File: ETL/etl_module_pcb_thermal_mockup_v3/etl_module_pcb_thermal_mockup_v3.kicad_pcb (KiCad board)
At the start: 2 copper layers, 44.1 x 57.5 mm, 21 parts, among them J1 WP7B-S050VA1-R8000, J2 WP7B-S050VA1-R8000, J3 Conn_02x02_Odd_Even, J4 Conn_02x08_Counter_Clockwise, J5 Conn_02x08_Counter_Clockwise, J6 Conn_02x08_Counter_Clockwise, J7 Conn_02x08_Counter_Clockwise

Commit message: Progress on etl_module_pcb_thermal_mcokup_v3
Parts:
- removed X1: , unl_silab:PCB_ETROC2_dummy
- added U1: ETROC_dummy_thermal_sensors, unl_silab:PCB_ETROC2_dummy, F.Cu at (11.2, 50.7)
- moved J7 24.2 mm to (33.3, 16.8)
- moved J4 19.4 mm to (9.40, 43.5)
- moved J6 18.2 mm to (11.4, 16.9)
- moved J5 8.65 mm to (33.2, 42.7)
- renumbered X2 to U2, X3 to U3, X4 to U4
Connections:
- J1 pad 10: /30_N -> unconnected-(J1-Pad10)
- J1 pad 11: /31_P -> unconnected-(J1-Pad11)
- J1 pad 12: /31_N -> unconnected-(J1-Pad12)
- J1 pad 13: /32_P -> unconnected-(J1-Pad13)
- J1 pad 14: /32_N -> unconnected-(J1-Pad14)
- J1 pad 15: /33_P -> unconnected-(J1-Pad15)
- J1 pad 16: /33_N -> unconnected-(J1-Pad16)
- J1 pad 17: /34_P -> unconnected-(J1-Pad17)
- J1 pad 18: /34_N -> unconnected-(J1-Pad18)
- J1 pad 19: /35_P -> unconnected-(J1-Pad19)
- J1 pad 2: /26_N -> unconnected-(J1-Pad2)
- J1 pad 20: /35_N -> unconnected-(J1-Pad20)
- J1 pad 21: /36_P -> unconnected-(J1-Pad21)
- J1 pad 22: /36_N -> unconnected-(J1-Pad22)
- J1 pad 23: /37_P -> unconnected-(J1-Pad23)
- J1 pad 24: /37_N -> unconnected-(J1-Pad24)
- J1 pad 25: /38_P -> unconnected-(J1-Pad25)
- J1 pad 26: /38_N -> unconnected-(J1-Pad26)
- J1 pad 27: /39_P -> unconnected-(J1-Pad27)
- J1 pad 28: /39_N -> unconnected-(J1-Pad28)
- J1 pad 29: /40_P -> unconnected-(J1-Pad29)
- J1 pad 3: /27_P -> unconnected-(J1-Pad3)
- J1 pad 30: /40_N -> unconnected-(J1-Pad30)
- J1 pad 31: /41_P -> unconnected-(J1-Pad31)
- J1 pad 32: /41_N -> unconnected-(J1-Pad32)
- J1 pad 33: /42_P -> unconnected-(J1-Pad33)
- J1 pad 34: /42_N -> unconnected-(J1-Pad34)
- J1 pad 35: /43_P -> unconnected-(J1-Pad35)
- J1 pad 36: /43_N -> unconnected-(J1-Pad36)
- J1 pad 37: /44_P -> unconnected-(J1-Pad37)
- J1 pad 38: /44_N -> unconnected-(J1-Pad38)
- J1 pad 39: /45_P -> unconnected-(J1-Pad39)
- J1 pad 4: /27_N -> unconnected-(J1-Pad4)
- J1 pad 40: /45_N -> unconnected-(J1-Pad40)
- J1 pad 41: /46_P -> unconnected-(J1-Pad41)
- J1 pad 42: /46_N -> unconnected-(J1-Pad42)
- J1 pad 43: /47_P -> unconnected-(J1-Pad43)
- J1 pad 44: /47_N -> unconnected-(J1-Pad44)
- J1 pad 45: /48_P -> unconnected-(J1-Pad45)
- J1 pad 46: /48_N -> unconnected-(J1-Pad46)
- J1 pad 47: /49_P -> unconnected-(J1-Pad47)
- J1 pad 48: /49_N -> unconnected-(J1-Pad48)
- J1 pad 49: /S2 -> unconnected-(J1-Pad49)
- J1 pad 5: /28_P -> unconnected-(J1-Pad5)
- J1 pad 50: /S2 -> unconnected-(J1-Pad50)
- J1 pad 6: /28_N -> unconnected-(J1-Pad6)
- J1 pad 7: /29_P -> unconnected-(J1-Pad7)
- J1 pad 8: /29_N -> unconnected-(J1-Pad8)
- J1 pad 9: /30_P -> unconnected-(J1-Pad9)
- J2 pad 1: /01_N -> unconnected-(J2-Pad1)
- J2 pad 10: /05_P -> unconnected-(J2-Pad10)
- J2 pad 11: /06_N -> unconnected-(J2-Pad11)
- J2 pad 12: /06_P -> unconnected-(J2-Pad12)
- J2 pad 13: /07_N -> unconnected-(J2-Pad13)
- J2 pad 14: /07_P -> unconnected-(J2-Pad14)
- J2 pad 15: /08_N -> unconnected-(J2-Pad15)
- J2 pad 16: /08_P -> unconnected-(J2-Pad16)
- J2 pad 17: /09_N -> unconnected-(J2-Pad17)
- J2 pad 18: /09_P -> unconnected-(J2-Pad18)
- J2 pad 19: /10_N -> unconnected-(J2-Pad19)
- J2 pad 2: /01_P -> unconnected-(J2-Pad2)
- J2 pad 20: /10_P -> unconnected-(J2-Pad20)
- J2 pad 21: /11_N -> unconnected-(J2-Pad21)
- J2 pad 22: /11_P -> unconnected-(J2-Pad22)
- J2 pad 23: /12_N -> unconnected-(J2-Pad23)
- J2 pad 24: /12_P -> unconnected-(J2-Pad24)
- J2 pad 25: /13_N -> unconnected-(J2-Pad25)
- J2 pad 26: /13_P -> unconnected-(J2-Pad26)
- J2 pad 27: /14_N -> unconnected-(J2-Pad27)
- J2 pad 28: /14_P -> unconnected-(J2-Pad28)
- J2 pad 29: /15_N -> unconnected-(J2-Pad29)
- J2 pad 3: /02_N -> unconnected-(J2-Pad3)
- J2 pad 30: /15_P -> unconnected-(J2-Pad30)
- J2 pad 31: /16_N -> unconnected-(J2-Pad31)
- J2 pad 32: /16_P -> unconnected-(J2-Pad32)
- J2 pad 33: /17_N -> unconnected-(J2-Pad33)
- J2 pad 34: /17_P -> unconnected-(J2-Pad34)
- J2 pad 35: /18_N -> unconnected-(J2-Pad35)
- J2 pad 36: /18_P -> unconnected-(J2-Pad36)
- J2 pad 37: /19_N -> unconnected-(J2-Pad37)
- J2 pad 38: /19_P -> unconnected-(J2-Pad38)
- J2 pad 39: /20_N -> unconnected-(J2-Pad39)
- J2 pad 4: /02_P -> unconnected-(J2-Pad4)
- J2 pad 40: /20_P -> unconnected-(J2-Pad40)
- J2 pad 41: /21_N -> unconnected-(J2-Pad41)
- J2 pad 42: /21_P -> unconnected-(J2-Pad42)
- J2 pad 43: /22_N -> unconnected-(J2-Pad43)
- J2 pad 44: /22_P -> unconnected-(J2-Pad44)
- J2 pad 45: /23_N -> unconnected-(J2-Pad45)
- J2 pad 46: /23_P -> unconnected-(J2-Pad46)
- J2 pad 47: /24_N -> unconnected-(J2-Pad47)
- J2 pad 48: /24_P -> unconnected-(J2-Pad48)
- J2 pad 49: /S1 -> unconnected-(J2-Pad49)
- J2 pad 5: /03_N -> unconnected-(J2-Pad5)
- J2 pad 50: /S1 -> unconnected-(J2-Pad50)
- J2 pad 6: /03_P -> unconnected-(J2-Pad6)
- J2 pad 7: /04_N -> unconnected-(J2-Pad7)
- J2 pad 8: /04_P -> unconnected-(J2-Pad8)
- J2 pad 9: /05_N -> unconnected-(J2-Pad9)
- J4 pad 1: unconnected-(J4-Pad1) -> /X1EBR2
- J4 pad 10: unconnected-(J4-Pad10) -> /X1LBL1
- J4 pad 11: unconnected-(J4-Pad11) -> /X1LBR1
- J4 pad 12: unconnected-(J4-Pad12) -> /X1LBL2
- J4 pad 13: unconnected-(J4-Pad13) -> /X1LTR2
- J4 pad 14: unconnected-(J4-Pad14) -> /X1LTL1
- J4 pad 15: unconnected-(J4-Pad15) -> /X1LTR1
- J4 pad 16: unconnected-(J4-Pad16) -> /X1LTL2
- J4 pad 2: unconnected-(J4-Pad2) -> /X1EBL1
- J4 pad 3: unconnected-(J4-Pad3) -> /X1EBR1
- J4 pad 4: unconnected-(J4-Pad4) -> /X1EBL2
- J4 pad 5: unconnected-(J4-Pad5) -> /X1ETR2
- J4 pad 6: unconnected-(J4-Pad6) -> /X1ETL1
- J4 pad 7: unconnected-(J4-Pad7) -> /X1ETR1
- J4 pad 8: unconnected-(J4-Pad8) -> /X1ETL2
- J4 pad 9: unconnected-(J4-Pad9) -> /X1LBR2
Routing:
- net /P1: track 3430.2 -> 0.00 mm, vias 12 -> 0
- net unconnected-(J6-Pad10): track 0.00 -> 3378.6 mm, vias 0 -> 12
- net /X1EBL1: track 0.00 -> 19.0 mm, vias 0 -> 1
- net /X1EBR2: track 0.00 -> 18.8 mm, vias 0 -> 1
- net /X1ETR2: track 0.00 -> 17.4 mm, vias 0 -> 1
- net /X1EBR1: track 0.00 -> 17.3 mm, vias 0 -> 1
- net /X1EBL2: track 0.00 -> 17.0 mm, vias 0 -> 1
- net /X1ETL1: track 0.00 -> 16.2 mm, vias 0 -> 1
- net /X1ETR1: track 0.00 -> 14.1 mm, vias 0 -> 1
- net /X1LBR1: track 0.00 -> 13.0 mm, vias 0 -> 1
- net /X1ETL2: track 0.00 -> 13.0 mm, vias 0 -> 1
- net /X1LBR2: track 0.00 -> 12.7 mm, vias 0 -> 1
- net /X1LBL2: track 0.00 -> 12.1 mm, vias 0 -> 1
- net /X1LBL1: track 0.00 -> 11.6 mm, vias 0 -> 1
- net /X1LTR2: track 0.00 -> 8.83 mm, vias 0 -> 1
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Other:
- copper layers 2 -> 4

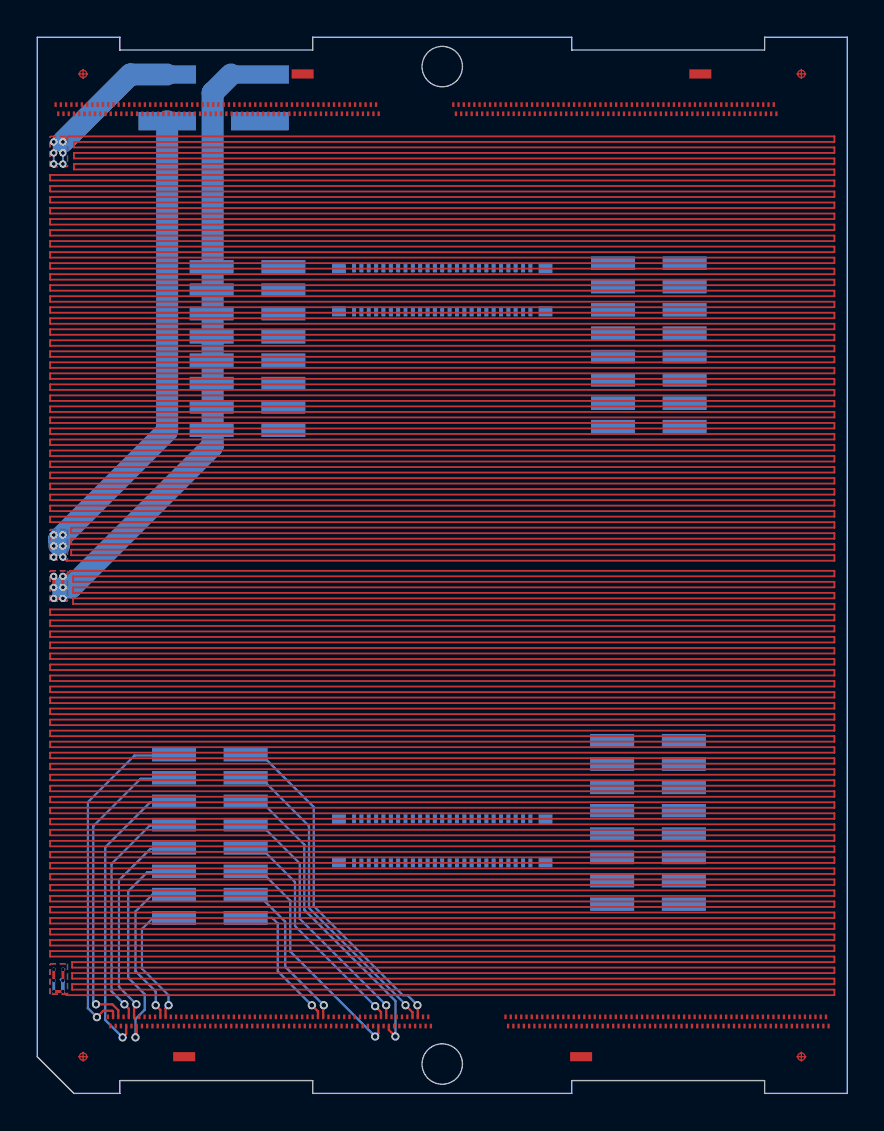
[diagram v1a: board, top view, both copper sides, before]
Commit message: Finishes first draft of etl_module_pcb_thermal_mockup_v3
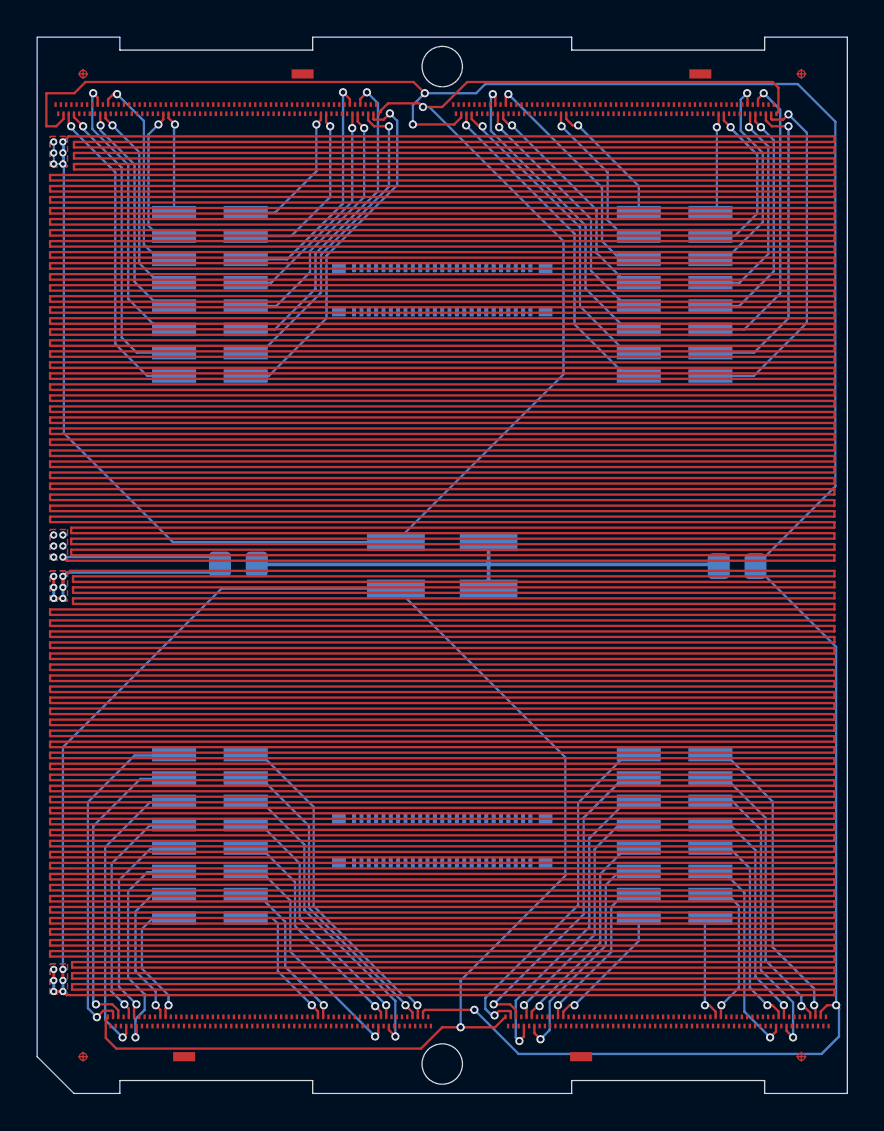
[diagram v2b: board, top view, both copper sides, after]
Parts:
- added JMPR1: 0, Resistor_SMD:R_0805_2012Metric_Pad1.20x1.40mm_HandSolder, B.Cu at (10.9, 28.7)
- added JMPR2: 0, Resistor_SMD:R_0805_2012Metric_Pad1.20x1.40mm_HandSolder, B.Cu at (38.1, 28.8)
- U2, U3, U4: value (none) -> ETROC_dummy_thermal_sensors
- moved J3 28.3 mm to (22.1, 28.8)
- moved J6 3.59 mm to (9.40, 14.0), turned to 0 degrees
- moved J7 3.09 mm to (34.7, 14.0), turned to 0 degrees
- moved J5 1.63 mm to (34.7, 43.5)
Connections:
- J3 pad 1: /P1 -> /GND
- J3 pad 2: /P2 -> /P1
- J3 pad 3: /P1 -> /GND
- J3 pad 4: /P2 -> /P1
- J5 pad 1: unconnected-(J5-Pad1) -> /X2EBR2
- J5 pad 10: unconnected-(J5-Pad10) -> /X2LBL1
- J5 pad 11: unconnected-(J5-Pad11) -> /X2LBR1
- J5 pad 12: unconnected-(J5-Pad12) -> /X2LBL2
- J5 pad 13: unconnected-(J5-Pad13) -> /X2LTR2
- J5 pad 14: unconnected-(J5-Pad14) -> /X2LTL1
- J5 pad 15: unconnected-(J5-Pad15) -> /X2LTR1
- J5 pad 16: unconnected-(J5-Pad16) -> /X2LTL2
- J5 pad 2: unconnected-(J5-Pad2) -> /X2EBL1
- J5 pad 3: unconnected-(J5-Pad3) -> /X2EBR1
- J5 pad 4: unconnected-(J5-Pad4) -> /X2EBL2
- J5 pad 5: unconnected-(J5-Pad5) -> /X2ETR2
- J5 pad 6: unconnected-(J5-Pad6) -> /X2ETL1
- J5 pad 7: unconnected-(J5-Pad7) -> /X2ETR1
- J5 pad 8: unconnected-(J5-Pad8) -> /X2ETL2
- J5 pad 9: unconnected-(J5-Pad9) -> /X2LBR2
- J6 pad 1: unconnected-(J6-Pad1) -> /X3EBR2
- J6 pad 10: unconnected-(J6-Pad10) -> /X3LBL1
- J6 pad 11: unconnected-(J6-Pad11) -> /X3LBR1
- J6 pad 12: unconnected-(J6-Pad12) -> /X3LBL2
- J6 pad 13: unconnected-(J6-Pad13) -> /X3LTR2
- J6 pad 14: unconnected-(J6-Pad14) -> /X3LTL1
- J6 pad 15: unconnected-(J6-Pad15) -> /X3LTR1
- J6 pad 16: unconnected-(J6-Pad16) -> /X3LTL2
- J6 pad 2: unconnected-(J6-Pad2) -> /X3EBL1
- J6 pad 3: unconnected-(J6-Pad3) -> /X3EBR1
- J6 pad 4: unconnected-(J6-Pad4) -> /X3EBL2
- J6 pad 5: unconnected-(J6-Pad5) -> /X3ETR2
- J6 pad 6: unconnected-(J6-Pad6) -> /X3ETL1
- J6 pad 7: unconnected-(J6-Pad7) -> /X3ETR1
- J6 pad 8: unconnected-(J6-Pad8) -> /X3ETL2
- J6 pad 9: unconnected-(J6-Pad9) -> /X3LBR2
- J7 pad 1: unconnected-(J7-Pad1) -> /X4EBR2
- J7 pad 10: unconnected-(J7-Pad10) -> /X4LBL1
- J7 pad 11: unconnected-(J7-Pad11) -> /X4LBR1
- J7 pad 12: unconnected-(J7-Pad12) -> /X4LBL2
- J7 pad 13: unconnected-(J7-Pad13) -> /X4LTR2
- J7 pad 14: unconnected-(J7-Pad14) -> /X4LTL1
- J7 pad 15: unconnected-(J7-Pad15) -> /X4LTR1
- J7 pad 16: unconnected-(J7-Pad16) -> /X4LTL2
- J7 pad 2: unconnected-(J7-Pad2) -> /X4EBL1
- J7 pad 3: unconnected-(J7-Pad3) -> /X4EBR1
- J7 pad 4: unconnected-(J7-Pad4) -> /X4EBL2
- J7 pad 5: unconnected-(J7-Pad5) -> /X4ETR2
- J7 pad 6: unconnected-(J7-Pad6) -> /X4ETL1
- J7 pad 7: unconnected-(J7-Pad7) -> /X4ETR1
- J7 pad 8: unconnected-(J7-Pad8) -> /X4ETL2
- J7 pad 9: unconnected-(J7-Pad9) -> /X4LBR2
- U1 pad 1: unconnected-(U1-Pad1) -> /P1
- U1 pad 121: unconnected-(U1-Pad121) -> /VSS
- U2 pad 1: (no net) -> /P1
- U2 pad 104: (no net) -> /X2LBR1
- U2 pad 105: (no net) -> /X2LBR2
- U2 pad 107: (no net) -> /X2ETR1
- U2 pad 108: (no net) -> /X2ETR2
- U2 pad 11: (no net) -> /X2LBL1
- U2 pad 117: (no net) -> /X2EBR1
- U2 pad 119: (no net) -> /X2EBR2
- U2 pad 12: (no net) -> /X2LBL2
- U2 pad 121: (no net) -> /VSS
- U2 pad 21: (no net) -> /X2LTL1
- U2 pad 23: (no net) -> /X2LTL2
- U2 pad 3: (no net) -> /X2EBL1
- U2 pad 5: (no net) -> /X2EBL2
- U2 pad 8: (no net) -> /X2ETL1
- U2 pad 81: (no net) -> /X2LTR1
- U2 pad 83: (no net) -> /X2LTR2
- U2 pad 9: (no net) -> /X2ETL2
- U3 pad 1: (no net) -> /P1
- U3 pad 104: (no net) -> /X3LBR1
- U3 pad 105: (no net) -> /X3LBR2
- U3 pad 107: (no net) -> /X3ETR1
- U3 pad 108: (no net) -> /X3ETR2
- U3 pad 11: (no net) -> /X3LBL1
- U3 pad 117: (no net) -> /X3EBR1
- U3 pad 119: (no net) -> /X3EBR2
- U3 pad 12: (no net) -> /X3LBL2
- U3 pad 121: (no net) -> /VSS
- U3 pad 21: (no net) -> /X3LTL1
- U3 pad 23: (no net) -> /X3LTL2
- U3 pad 3: (no net) -> /X3EBL1
- U3 pad 5: (no net) -> /X3EBL2
- U3 pad 8: (no net) -> /X3ETL1
- U3 pad 81: (no net) -> /X3LTR1
- U3 pad 83: (no net) -> /X3LTR2
- U3 pad 9: (no net) -> /X3ETL2
- U4 pad 1: (no net) -> /P1
- U4 pad 104: (no net) -> /X4LBR1
- U4 pad 105: (no net) -> /X4LBR2
- U4 pad 107: (no net) -> /X4ETR1
- U4 pad 108: (no net) -> /X4ETR2
- U4 pad 11: (no net) -> /X4LBL1
- U4 pad 117: (no net) -> /X4EBR1
- U4 pad 119: (no net) -> /X4EBR2
- U4 pad 12: (no net) -> /X4LBL2
- U4 pad 121: (no net) -> /VSS
- U4 pad 21: (no net) -> /X4LTL1
- U4 pad 23: (no net) -> /X4LTL2
- U4 pad 3: (no net) -> /X4EBL1
- U4 pad 5: (no net) -> /X4EBL2
- U4 pad 8: (no net) -> /X4ETL1
- U4 pad 81: (no net) -> /X4LTR1
- U4 pad 83: (no net) -> /X4LTR2
- U4 pad 9: (no net) -> /X4ETL2
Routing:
- net /P1: track 0.00 -> 6881.7 mm, vias 0 -> 26
- net unconnected-(J6-Pad10): track 3378.6 -> 0.00 mm, vias 12 -> 0
- net /P2: track 3373.9 -> 0.00 mm, vias 12 -> 0
- net /VSS: track 0.00 -> 132.0 mm, vias 0 -> 4
- net /GND: track 0.00 -> 27.8 mm
- net /X3EBL1: track 0.00 -> 19.9 mm, vias 0 -> 1
- net /X2EBL1: track 0.00 -> 19.6 mm, vias 0 -> 1
- net /X4EBL1: track 0.00 -> 19.6 mm, vias 0 -> 1
- net /X4EBR2: track 0.00 -> 18.6 mm, vias 0 -> 1
- net /X3ETL1: track 0.00 -> 17.9 mm, vias 0 -> 1
- net /X2EBL2: track 0.00 -> 17.8 mm, vias 0 -> 1
- net /X3EBL2: track 0.00 -> 17.7 mm, vias 0 -> 1
- net /X3EBR2: track 0.00 -> 17.5 mm, vias 0 -> 1
- net /X4EBR1: track 0.00 -> 17.3 mm, vias 0 -> 1
- net /X2ETL1: track 0.00 -> 17.2 mm, vias 0 -> 1
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- removed copper zone on B.Cu, net /P2
- removed copper zone on F.Cu, net /P2

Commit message: Reworking of etl_module_pcb_thermal_mockup_v3 to embed ADCs for easier monitoring
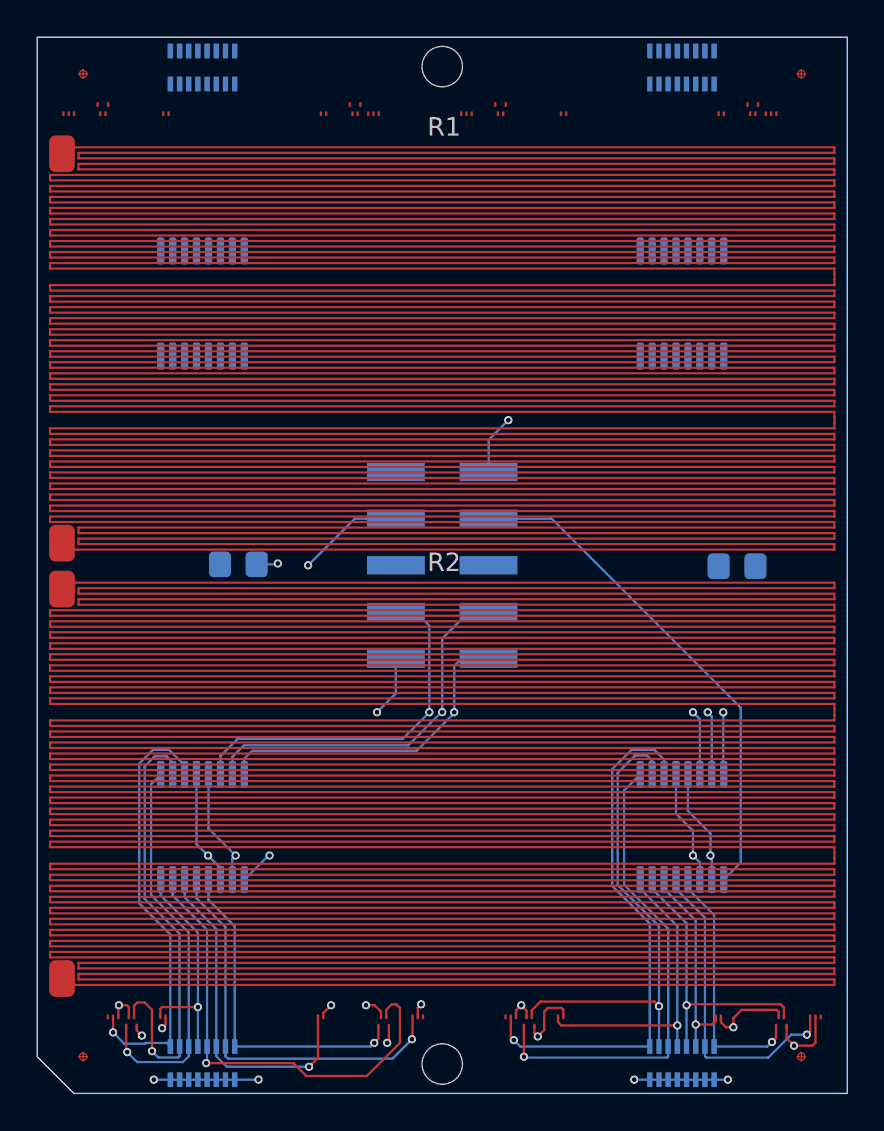
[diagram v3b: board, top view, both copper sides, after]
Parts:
- removed J1, J2: WP7B-S050VA1-R8000, SamacSys_Parts:WP7BS050VA1R8000
- removed J4, J5, J6, J7: Conn_02x08_Counter_Clockwise, Connector_PinHeader_1.27mm:PinHeader_2x08_P1.27mm_Vertical_SMD
- removed the REF** at (8.00, 55.5)
- removed the REF** at (29.6, 55.5)
- removed the REF** at (36.1, 2.00)
- removed the REF** at (14.4, 2.00)
- added R1: 12.6, unl_silab:ETROC_Heater_Serpantine, F.Cu at (22.1, 5.39)
- added R2: 12.6, unl_silab:ETROC_Heater_Serpantine, F.Cu at (22.1, 29.1)
- added RN1: 10k, Resistor_SMD:R_Array_Convex_8x0602, B.Cu at (9.00, 55.9)
- added RN2: 10k, Resistor_SMD:R_Array_Convex_8x0602, B.Cu at (35.1, 55.9)
- added RN3: 10k, Resistor_SMD:R_Array_Convex_8x0602, B.Cu at (9.00, 1.65)
- added RN4: 10k, Resistor_SMD:R_Array_Convex_8x0602, B.Cu at (35.1, 1.65)
- added U5: ADC088SO22, Package_SO:TSSOP-16_4.4x5mm_P0.65mm, B.Cu at (9.00, 43.0)
- added U6: ADC088SO22, Package_SO:TSSOP-16_4.4x5mm_P0.65mm, B.Cu at (35.1, 43.0)
- added U7: ADC088SO22, Package_SO:TSSOP-16_4.4x5mm_P0.65mm, B.Cu at (9.00, 14.5)
- added U8: ADC088SO22, Package_SO:TSSOP-16_4.4x5mm_P0.65mm, B.Cu at (35.1, 14.5)
- J3: value Conn_02x02_Odd_Even -> Conn_02x05_Counter_Clockwise; footprint Connector_PinHeader_2.54mm:PinHeader_2x02_P2.54mm_Vertical_SMD -> Connector_PinHeader_2.54mm:PinHeader_2x05_P2.54mm_Vertical_SMD
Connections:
- J3 pad 1: /GND -> /CS4
- J3 pad 2: /P1 -> /CS3
- J3 pad 3: /GND -> /CS2
- J3 pad 4: /P1 -> /CS1
- JMPR1 pad 1: /P1 -> Net-(JMPR1-Pad1)
- JMPR1 pad 2: /GND -> GND
- JMPR2 pad 1: /GND -> GND
- U1 pad 1: /P1 -> VCC
- U1 pad 104: /X1LBR1 -> Net-(RN1-Pad16)
- U1 pad 105: /X1LBR2 -> GND
- U1 pad 107: /X1ETR1 -> Net-(RN1-Pad13)
- U1 pad 108: /X1ETR2 -> GND
- U1 pad 11: /X1LBL1 -> Net-(RN1-Pad10)
- U1 pad 117: /X1EBR1 -> Net-(RN1-Pad15)
- U1 pad 119: /X1EBR2 -> GND
- U1 pad 12: /X1LBL2 -> GND
- U1 pad 21: /X1LTL1 -> Net-(RN1-Pad12)
- U1 pad 23: /X1LTL2 -> GND
- U1 pad 3: /X1EBL1 -> Net-(RN1-Pad9)
- U1 pad 5: /X1EBL2 -> GND
- U1 pad 8: /X1ETL1 -> Net-(RN1-Pad11)
- U1 pad 81: /X1LTR1 -> Net-(RN1-Pad14)
- U1 pad 83: /X1LTR2 -> GND
- U1 pad 9: /X1ETL2 -> GND
- U2 pad 1: /P1 -> VCC
- U2 pad 104: /X2LBR1 -> Net-(RN2-Pad16)
- U2 pad 105: /X2LBR2 -> GND
- U2 pad 107: /X2ETR1 -> Net-(RN2-Pad13)
- U2 pad 108: /X2ETR2 -> GND
- U2 pad 11: /X2LBL1 -> Net-(RN2-Pad10)
- U2 pad 117: /X2EBR1 -> Net-(RN2-Pad15)
- U2 pad 119: /X2EBR2 -> GND
- U2 pad 12: /X2LBL2 -> GND
- U2 pad 21: /X2LTL1 -> Net-(RN2-Pad12)
- U2 pad 23: /X2LTL2 -> GND
- U2 pad 3: /X2EBL1 -> Net-(RN2-Pad9)
- U2 pad 5: /X2EBL2 -> GND
- U2 pad 8: /X2ETL1 -> Net-(RN2-Pad11)
- U2 pad 81: /X2LTR1 -> Net-(RN2-Pad14)
- U2 pad 83: /X2LTR2 -> GND
- U2 pad 9: /X2ETL2 -> GND
- U3 pad 1: /P1 -> VCC
- U3 pad 104: /X3LBR1 -> /X3LBR
- U3 pad 105: /X3LBR2 -> GND
- U3 pad 107: /X3ETR1 -> /X3ETR
- U3 pad 108: /X3ETR2 -> GND
- U3 pad 11: /X3LBL1 -> /X3LBL
- U3 pad 117: /X3EBR1 -> /X3EBR
- U3 pad 119: /X3EBR2 -> GND
- U3 pad 12: /X3LBL2 -> GND
- U3 pad 21: /X3LTL1 -> /X3LTL
- U3 pad 23: /X3LTL2 -> GND
- U3 pad 3: /X3EBL1 -> /X3EBL
- U3 pad 5: /X3EBL2 -> GND
- U3 pad 8: /X3ETL1 -> /X3ETL
- U3 pad 81: /X3LTR1 -> /X3LTR
- U3 pad 83: /X3LTR2 -> GND
- U3 pad 9: /X3ETL2 -> GND
- U4 pad 1: /P1 -> VCC
- U4 pad 104: /X4LBR1 -> /X4LBR
- U4 pad 105: /X4LBR2 -> GND
- U4 pad 107: /X4ETR1 -> /X4ETR
- U4 pad 108: /X4ETR2 -> GND
- U4 pad 11: /X4LBL1 -> /X4LBL
- U4 pad 117: /X4EBR1 -> /X4EBR
- U4 pad 119: /X4EBR2 -> GND
- U4 pad 12: /X4LBL2 -> GND
- U4 pad 21: /X4LTL1 -> /X4LTL
- U4 pad 23: /X4LTL2 -> GND
- U4 pad 3: /X4EBL1 -> /X4EBL
- U4 pad 5: /X4EBL2 -> GND
- U4 pad 8: /X4ETL1 -> /X4ETL
- U4 pad 81: /X4LTR1 -> /X4LTR
- U4 pad 83: /X4LTR2 -> GND
- U4 pad 9: /X4ETL2 -> GND
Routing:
- net /P1: track 6881.7 -> 0.00 mm, vias 26 -> 0
- net /VSS: track 132.0 -> 0.00 mm, vias 4 -> 0
- net /DOUT: track 0.00 -> 39.6 mm, vias 0 -> 2
- net /DIN: track 0.00 -> 39.3 mm, vias 0 -> 2
- net GND: track 0.00 -> 37.5 mm, vias 0 -> 15
- net /CLK: track 0.00 -> 36.9 mm, vias 0 -> 2
- net Net-(RN2-Pad9): track 0.00 -> 29.1 mm, vias 0 -> 1
- net /GND: track 27.8 -> 0.00 mm
- net /CS2: track 0.00 -> 27.7 mm
- net Net-(RN2-Pad10): track 0.00 -> 26.6 mm, vias 0 -> 1
- net Net-(RN2-Pad11): track 0.00 -> 26.3 mm, vias 0 -> 1
- net Net-(RN1-Pad13): track 0.00 -> 25.6 mm, vias 0 -> 1
- net /CS1: track 0.00 -> 24.9 mm, vias 0 -> 2
- net Net-(RN1-Pad10): track 0.00 -> 24.9 mm, vias 0 -> 1
- net Net-(RN1-Pad9): track 0.00 -> 24.1 mm, vias 0 -> 1
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- added copper zone on In1.Cu, net +5V
- added copper zone on In2.Cu, net GND
- removed copper zone on B.Cu, net /P1
- removed copper zone on F.Cu, net /P1
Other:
- outline, holes or cut-outs redrawn
